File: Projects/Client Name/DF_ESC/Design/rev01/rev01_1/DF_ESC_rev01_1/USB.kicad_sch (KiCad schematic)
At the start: 0 parts

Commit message: Update 2024-02-03
Schematic finish but DRC CHEK Errors
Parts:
- added J6: USB_C_Receptacle_USB2.0, DF_ESC_Footprint_Library_Casa:USB-C_SMD-TYPE-C-31-M-12, symbol DF_ESC_Symbol_Library_Casa:USB_C_Receptacle_USB2.0
- added R56, R57, R58: 0R, Resistor_SMD:R_0603_1608Metric_Pad0.98x0.95mm_HandSolder, symbol Device:R
- added R59, R60: 5k1, Resistor_SMD:R_0603_1608Metric_Pad0.98x0.95mm_HandSolder, symbol Device:R
- added R61, R62: 22R, Resistor_SMD:R_0603_1608Metric_Pad0.98x0.95mm_HandSolder, symbol Device:R
- added U11: PUSB3AB6Z, DF_ESC_Footprint_Library_Casa:XSON-7_L2.2-W1.2-P0.50-BL, symbol DF_ESC_Symbol_Library_Casa:PUSB3AB6Z
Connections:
- new net: J6.S1 (SHIELD), J6.S2 (SHIELD), R56.1, R57.1
- new net +5V: R58.1
- new net +5V_C: J6.A4 (VBUS), J6.A9 (VBUS), J6.B4 (VBUS), J6.B9 (VBUS), R58.2, U11.3 (CH2), U11.5 (CH4)
- new net CC1: J6.A5 (CC1), R60.1, U11.1 (CH1)
- new net CC2: J6.B5 (CC2), R59.1, U11.4 (CH3)
- new net GND: J6.A1 (GND), J6.A12 (GND), J6.B1 (GND), J6.B12 (GND), R56.2, R57.2, R59.2, R60.2, U11.2 (GND)
- new net USB-C_N: J6.A7 (D-), J6.B7 (D-), R61.1, U11.6 (CH5)
- new net USB-C_P: J6.A6 (D+), J6.B6 (D+), R62.1, U11.7 (CH6)
- new net USB_N: R61.2
- new net USB_P: R62.2
- no-connect marks 0 -> 2
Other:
- note added: "ESD PROTECTION PLACE AS CLOSE AS POSSIBLE TO THE CONNECTOR"
- note added: "FIT A ZERO OHM LINK, CAP OR RESISTOR."
- note added: "PULL-DOWN TELL DE HOST WE ARE UFP. ONLY ONE USED AT GIVEN TIME. BOTH NECESSARY FOR REVERSIBILITY."
- note added: "ROUTE AS A DIFFERENTIAL PAIR"
- note added: "TERMINATING RESISTORS PLACE AS CLOSE AS POSSIBLE TO MCU"
- note added: "USB TYPE-C ONLY 2.0"
- note added: "[9] - USB"
- note removed: "[8] - MECHANICAL kjlkjlkjlk"

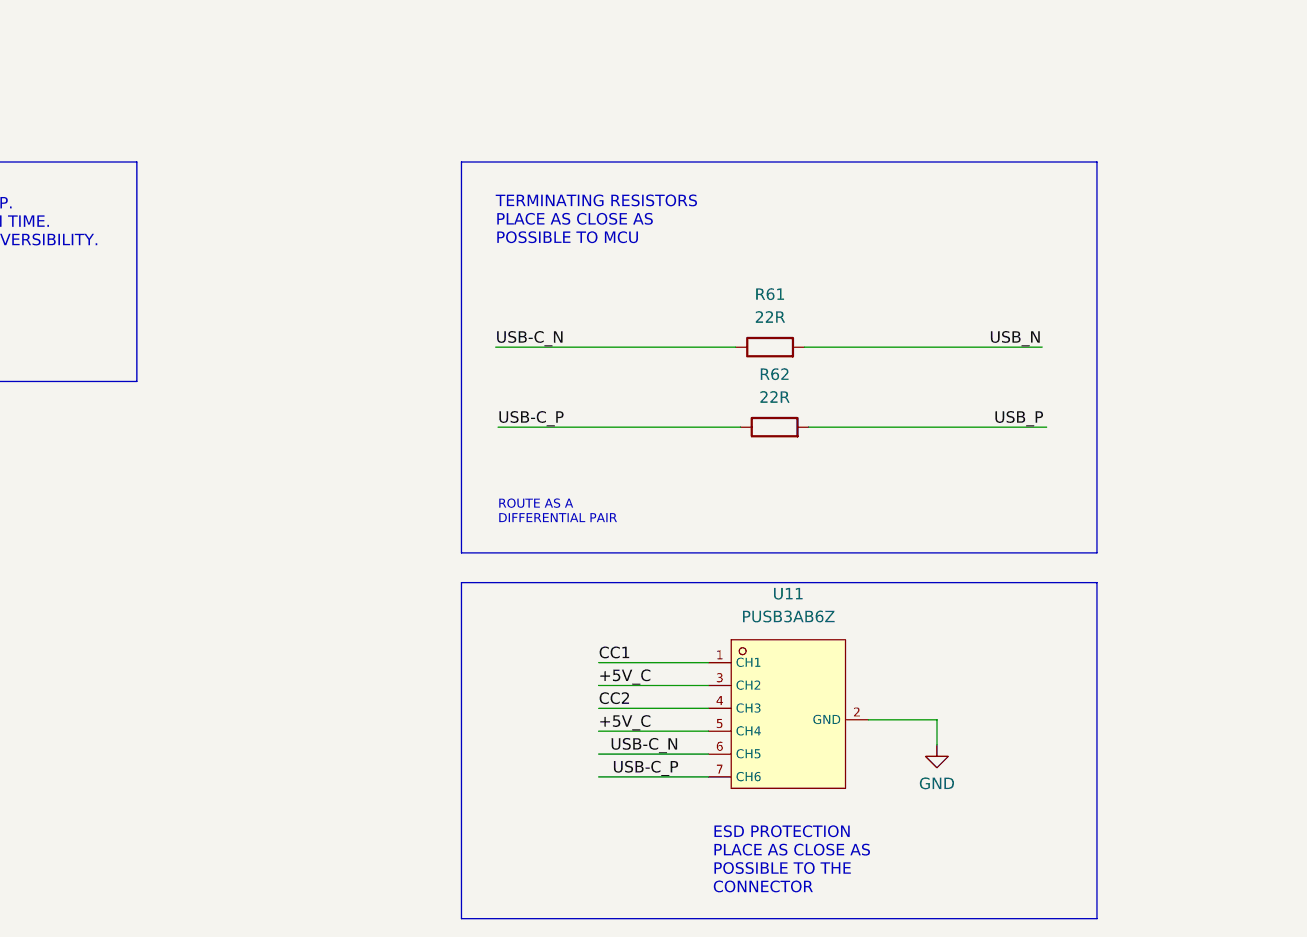
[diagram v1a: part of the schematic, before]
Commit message: Update 2024-03-03
ERC 0 Errors. Update PCB from schematics prepare to going on
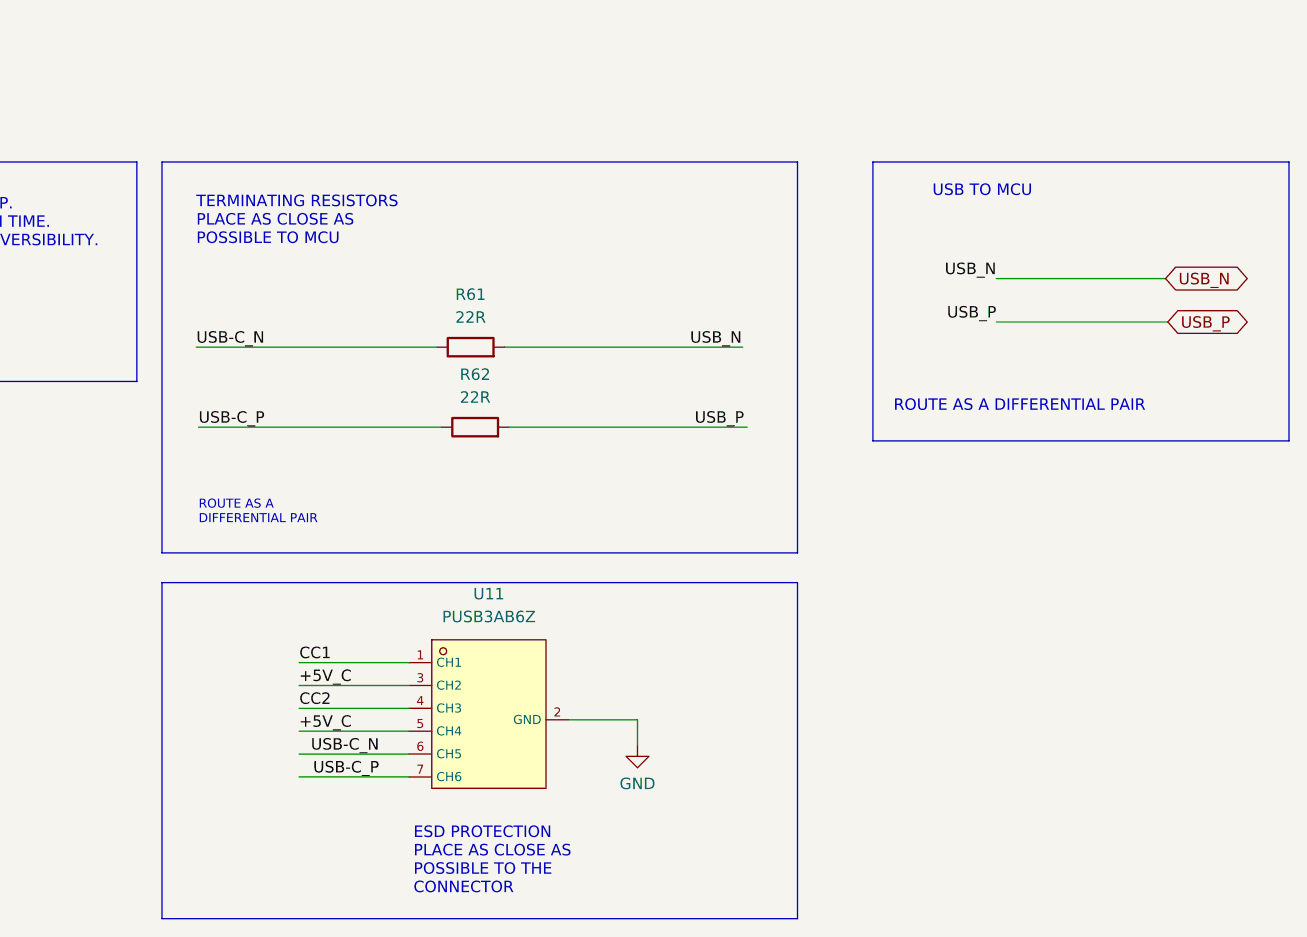
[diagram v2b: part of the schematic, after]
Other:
- note added: "USB TO MCU"
- moved on the sheet: R61, R62, U11

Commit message: Update 2024-03-03_2
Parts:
- renumbered J6 to J8, R56 to R53, R57 to R54, R58 to R55, R59 to R56, R60 to R57, R61 to R58, R62 to R59, U11 to U10
